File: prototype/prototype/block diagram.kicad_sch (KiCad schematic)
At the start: 38 parts, among them J1 Conn_01x06_Pin, J2 Screw_Terminal_01x02, Q1 2N7002, Q2 AO3400, Q3 2N7002, Q4 2N7002, U1 AMS1117-3.3, U11 ESP32-WROOM-32E, U5 MQ-5, U8 CI121S021 [adc]

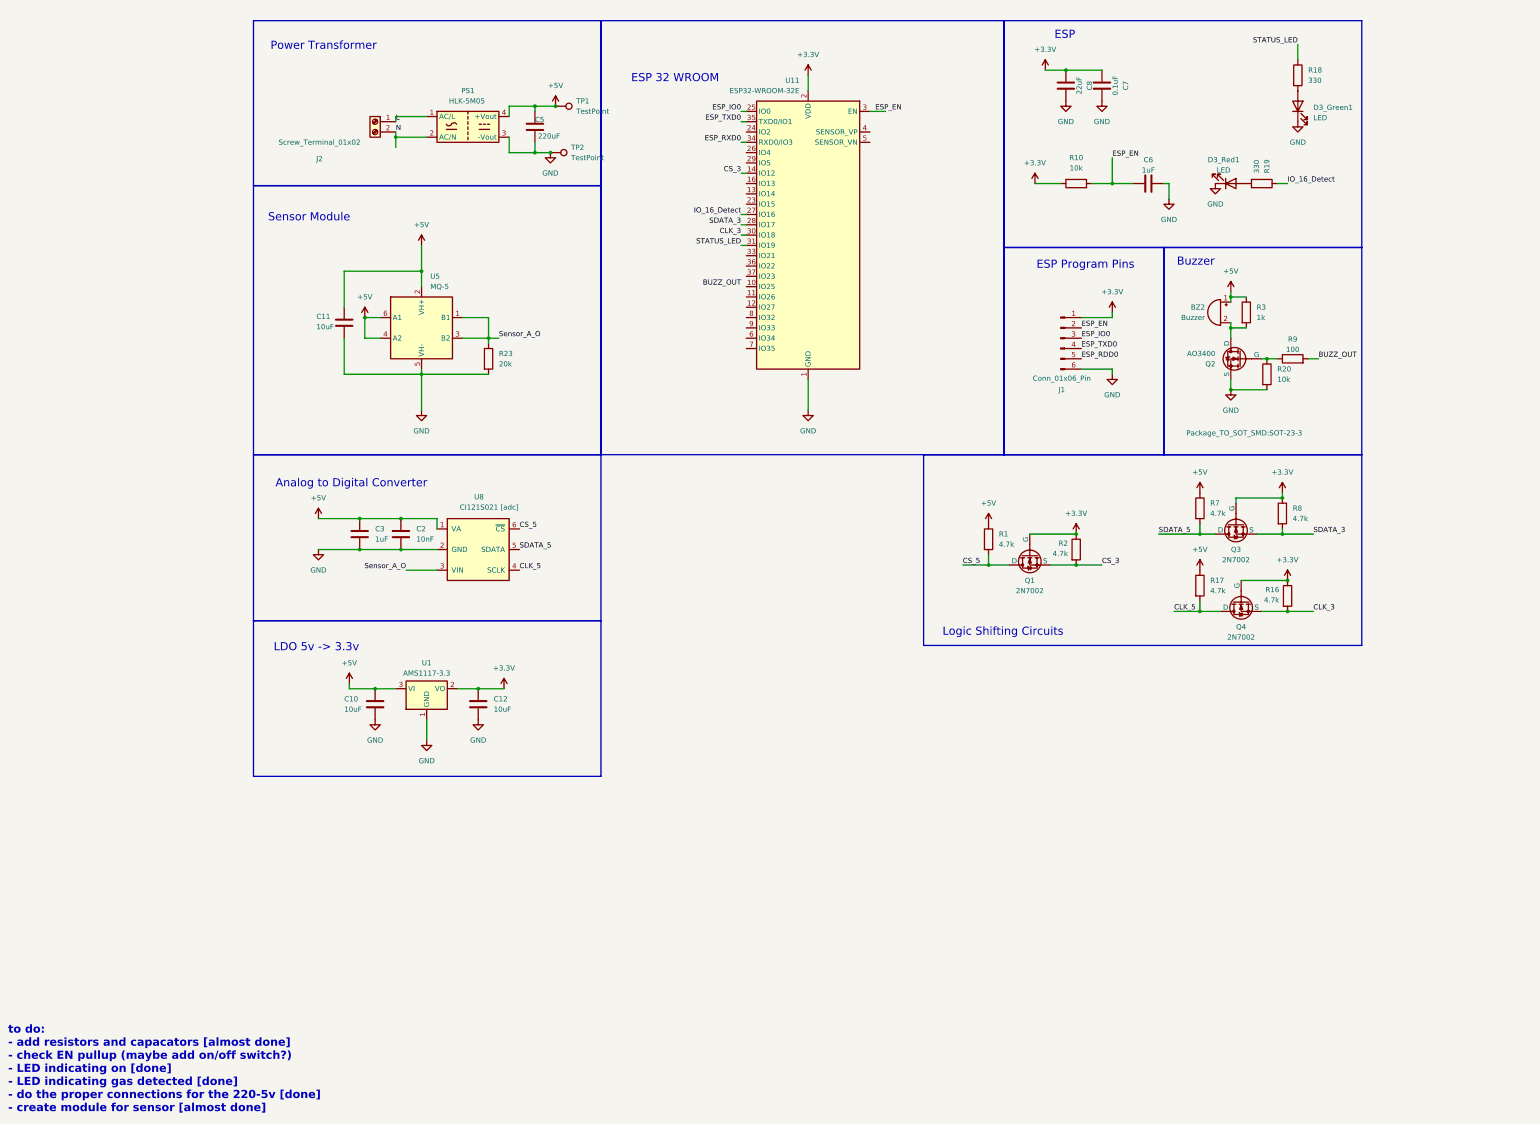
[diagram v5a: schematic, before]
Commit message: pcb layout and updated led
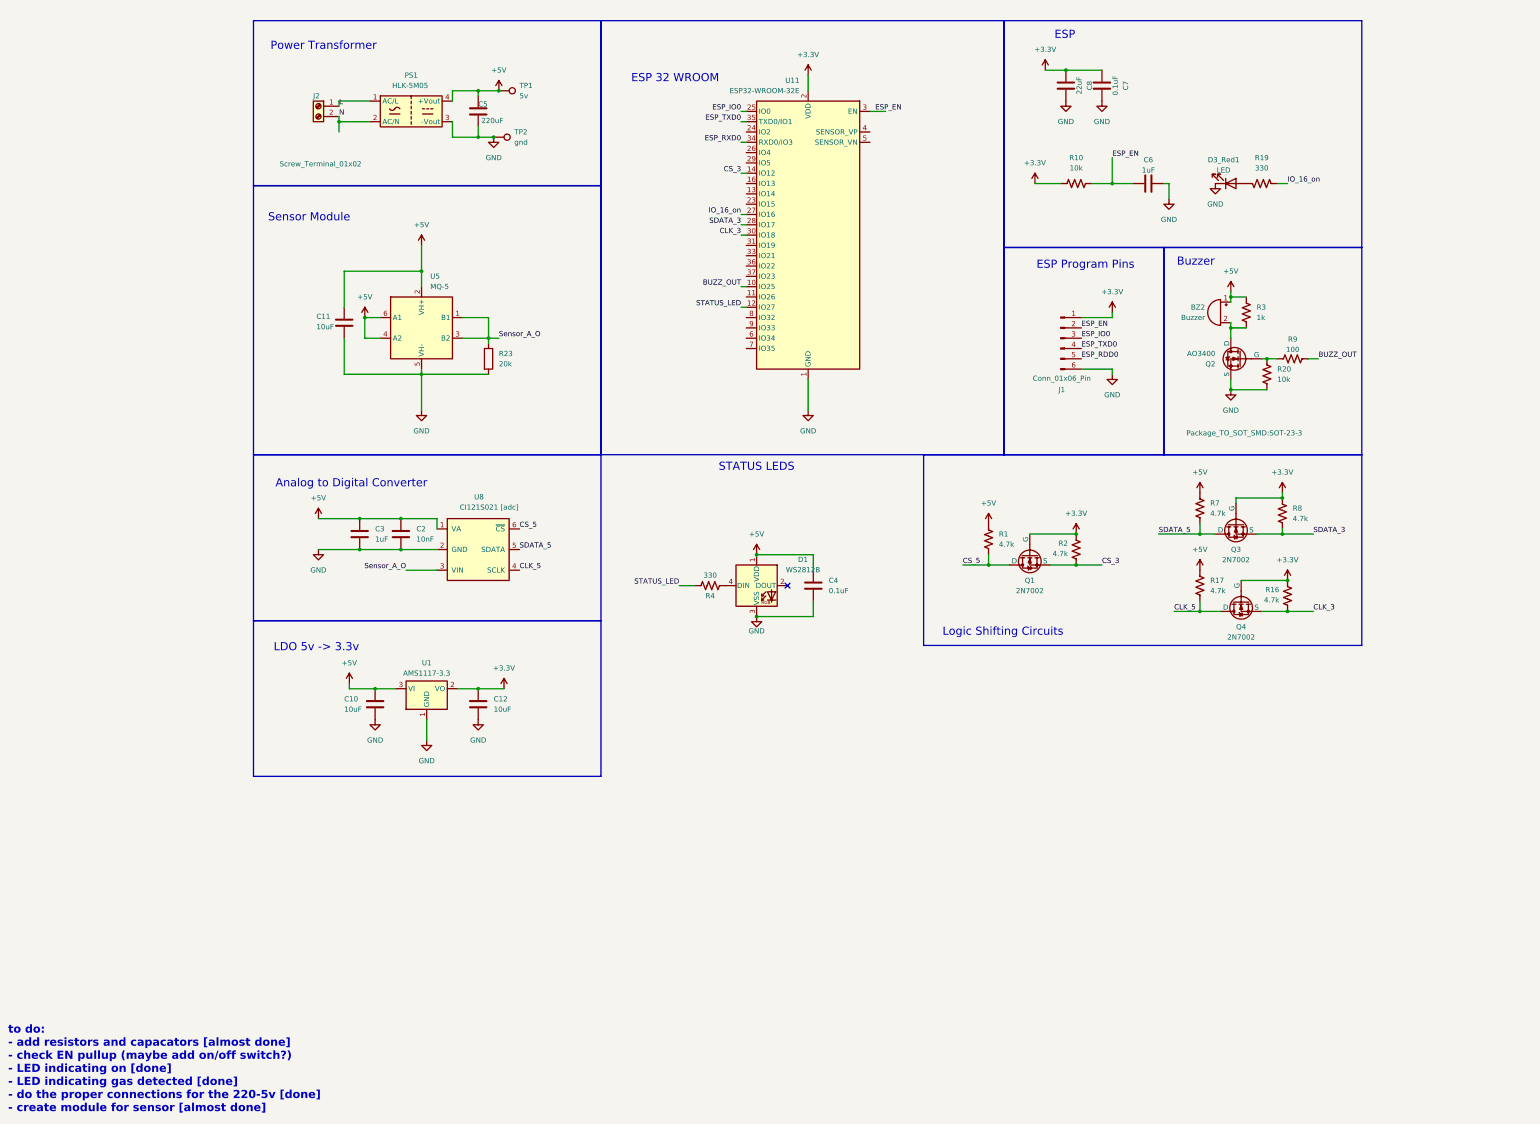
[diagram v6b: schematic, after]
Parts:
- removed D3_Green1: LED, symbol Device:LED
- removed R18: 330, Photon:R_0603_1608Metric_Pad0.98x0.95mm_HandSolder, symbol Device:R
- added C4: 0.1uF, Photon:C_0805_2012Metric, symbol Photon2:C_0.1u_0805_YAGEO
- added D1: WS2812B, LED_SMD:LED_WS2812B_PLCC4_5.0x5.0mm_P3.2mm, symbol LED:WS2812B
- added R4: 330, Photon:R_0805_2012Metric, symbol Photon2:R_330_0805_YAGEO
- BZ2: footprint (none) -> Photon:Buzzer_TDK_PS1240P02BT_D12.2mm_H6.5mm
- C10, C11, C12: footprint Photon:C0603 -> Photon:C_0805_2012Metric; symbol Device:C -> Photon2:C_10u_0805_SAMSUNG; LCSC (none) -> C1713; MPN (none) -> CL21A106KOQNNNE
- C2: footprint Photon:C0603 -> Photon:C_0805_2012Metric; symbol Device:C -> Photon2:C_10nF_0805_YAGEO; LCSC (none) -> C527200; MPN (none) -> CC0805JKNPO7BN103; Manufacturer (none) -> YAGEO; Package (none) -> 0805
- C3, C6: footprint Photon:C0603 -> Photon:C_0805_2012Metric; symbol Device:C -> Photon2:C_1uF_0805_MURATA; LCSC (none) -> C77083; MPN (none) -> GRM21BR71H105KA12L
- C5: footprint Photon:C0603 -> Photon:CP_Radial_D8.0mm_P3.50mm; symbol Device:C -> Photon2:C_220u_TH_HRK; LCSC (none) -> C2960236; MPN (none) -> 35V220uF CD110
- C7: footprint Photon:C0603 -> Photon:C_0805_2012Metric; symbol Device:C -> Photon2:C_0.1u_0805_YAGEO; LCSC (none) -> C520082; MPN (none) -> CC0805JRX7R7BB104
- C8: footprint Photon:C0603 -> Photon:C_1206_3216Metric_Pad1.33x1.80mm_HandSolder; symbol Device:C -> Photon2:C_22u_1206_SAMSUNG; LCSC (none) -> C5672; MPN (none) -> CL31A226KPHNNNE; Manufacturer (none) -> Chinocera; Package (none) -> 0805
- D3_Red1: footprint (none) -> Photon:LED-SMD_L2.0-W1.25-RD-GREEN
- J1: footprint (none) -> Connector_Hirose:Hirose_DF13-06P-1.25DS_1x06_P1.25mm_Horizontal
- R1, R16, R17, R2, R7, R8: footprint Photon:R_0603_1608Metric_Pad0.98x0.95mm_HandSolder -> Photon:R_0805_2012Metric; symbol Device:R -> Photon2:R_4.7k_0805_YAGEO; LCSC (none) -> C4176634; MPN (none) -> RC0805FR-134K7L
- R10, R20: footprint Photon:R_0603_1608Metric_Pad0.98x0.95mm_HandSolder -> Photon:R_0805_2012Metric; symbol Device:R -> Photon2:R_10k_0805_UNI-ROYAL; LCSC (none) -> C17414; MPN (none) -> 0805W8F1002T5E
- R19: footprint Photon:R_0603_1608Metric_Pad0.98x0.95mm_HandSolder -> Photon:R_0805_2012Metric; symbol Device:R -> Photon2:R_330_0805_YAGEO; LCSC (none) -> C4262771; MPN (none) -> RC0805FR-13330RL
- R3: footprint Photon:R_0603_1608Metric_Pad0.98x0.95mm_HandSolder -> Photon:R_0805_2012Metric; symbol Device:R -> Photon2:R_1k_0805_RALEC; LCSC (none) -> C103913; MPN (none) -> RTT05102JTP
- R9: footprint Photon:R_0603_1608Metric_Pad0.98x0.95mm_HandSolder -> Photon:R_0805_2012Metric_Pad1.20x1.40mm_HandSolder; symbol Device:R -> Photon2:R_100_0805_YAGEO; LCSC (none) -> C723351; MPN (none) -> RC0805FR-7W100RL
- TP1: value TestPoint -> 5v
- TP2: value TestPoint -> gnd
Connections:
- net +5V: now also C4.1, D1.1 (VDD)
- net BUZZ_OUT: now also U11.10 (IO25)
- net GND: now also C4.2, D1.3 (VSS)
- net STATUS_LED: now also U11.12 (IO27), R4.1; no longer U11.31 (IO19)
- net IO_16_Detect renamed IO_16_on
- new net: D1.4 (DIN), R4.2
- no-connect marks 0 -> 1
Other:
- note added: "STATUS LEDS"
- moved on the sheet: C5, J2, PS1, TP1, TP2

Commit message: pcb layout almost complete
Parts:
- R23: footprint Photon:R_0603_1608Metric_Pad0.98x0.95mm_HandSolder -> Photon:R_0805_2012Metric; symbol Device:R -> Photon2:R_22k_0805_VO; LCSC (none) -> C3017862; MPN (none) -> SCR0805J22K
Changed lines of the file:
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@@
 	)
 	(symbol
-		(lib_id "Device:R")
+		(lib_id "Photon2:R_22k_0805_VO")
 		(at 69.85 95.25 0)
 		(unit 1)
@@
 			)
 		)
-		(property "Footprint" "Photon:R_0603_1608Metric_Pad0.98x0.95mm_HandSolder"
-			(at 68.072 95.25 90)
+		(property "Footprint" "Photon:R_0805_2012Metric"
+			(at 70.866 95.504 90)
 			(effects
 				(font
@@
 			)
 		)
-		(property "Description" "Resistor"
+		(property "Description" "125mW Thick Film Resistor ±100ppm/℃ ±1% 330Ω 0805 Chip Resistor - Surface Mount ROHS"
 			(at 69.85 95.25 0)
 			(effects
+				(font
+					(size 1.27 1.27)
+				)
+				(hide yes)
+			)
+		)
+		(property "MPN" "SCR0805J22K"
+			(at 69.85 95.25 0)
+			(effects
+				(font
+					(size 1.27 1.27)
+				)
+				(hide yes)
+			)
+		)
+		(property "LCSC" "C3017862"
+			(at 69.85 95.25 0)
+			(effects

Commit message: editing pcb layout (desktop)
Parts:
- added TP3: 3v3, TestPoint:TestPoint_Keystone_5000-5004_Miniature, symbol Connector:TestPoint
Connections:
- net +3.3V: now also TP3.1
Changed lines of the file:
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@@
 	)
 	(junction
+		(at 73.66 176.53)
+		(diameter 0)
+		(color 0 0 0 0)
+	)
+	(junction
 		(at 266.7 149.86)
 		(diameter 0)
@@
 	(wire
 		(pts
+			(xy 73.66 176.53) (xy 74.93 176.53)
+		)
+		(stroke
+			(width 0)
+			(type default)
+		)
+	)
+	(wire
+		(pts
 			(xy 163.83 34.29) (xy 167.64 34.29)
 		)
@@
 					(unit 1)
 				)
+			)
+		)
+	)
+	(symbol
+		(lib_id "Connector:TestPoint")
+		(at 74.93 176.53 270)
+		(unit 1)
+		(exclude_from_sim no)
+		(in_bom yes)
+		(on_board yes)
+		(dnp no)
+		(fields_autoplaced yes)
+		(property "Reference" "TP3"
+			(at 80.01 175.2599 90)
+			(effects
+				(font
+					(size 1.27 1.27)
+				)
+				(justify left)
+			)
+		)
+		(property "Value" "3v3"
+			(at 80.01 177.7999 90)
+			(effects
+				(font
+					(size 1.27 1.27)
+				)
+				(justify left)
+			)
+		)
+		(property "Footprint" "TestPoint:TestPoint_Keystone_5000-5004_Miniature"
+			(at 74.93 181.61 0)
+			(effects
+				(font
+					(size 1.27 1.27)
+				)
+				(hide yes)
+			)
+		)
+		(property "Datasheet" "~"
+			(at 74.93 181.61 0)
+			(effects
+				(font
+					(size 1.27 1.27)
+				)
+				(hide yes)
+			)
+		)
+		(property "Description" "test point"
+			(at 74.93 176.53 0)
+			(effects
+				(font
+					(size 1.27 1.27)
+				)
+				(hide yes)
+			)
+		)
+		(pin "1"
+		)
+		(instances
+			(project "block diagram"
+				(path "/290c0625-1e23-4ef7-8910-f1eb5378fd87"
+					(reference "TP3")
+					(unit 1)
+				)
